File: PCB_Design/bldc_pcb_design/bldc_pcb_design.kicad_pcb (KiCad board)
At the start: 2 copper layers, 78.5 x 78.5 mm, 66 parts, among them IC1 DRV8305NPHPR, J1 Conn_01x04_Female, SW1 BOOT, SW2 RESET, U1 ESP32-WROOM-32D, U10 DS18S20Z+, U2 AS5600-ASOT, U3 LM2672M-3.3, U4 CSD18532NQ5B, U5 CSD18532NQ5B, U6 CSD18532NQ5B, U7 CSD18532NQ5B, U8 CSD18532NQ5B, U9 CSD18532NQ5B

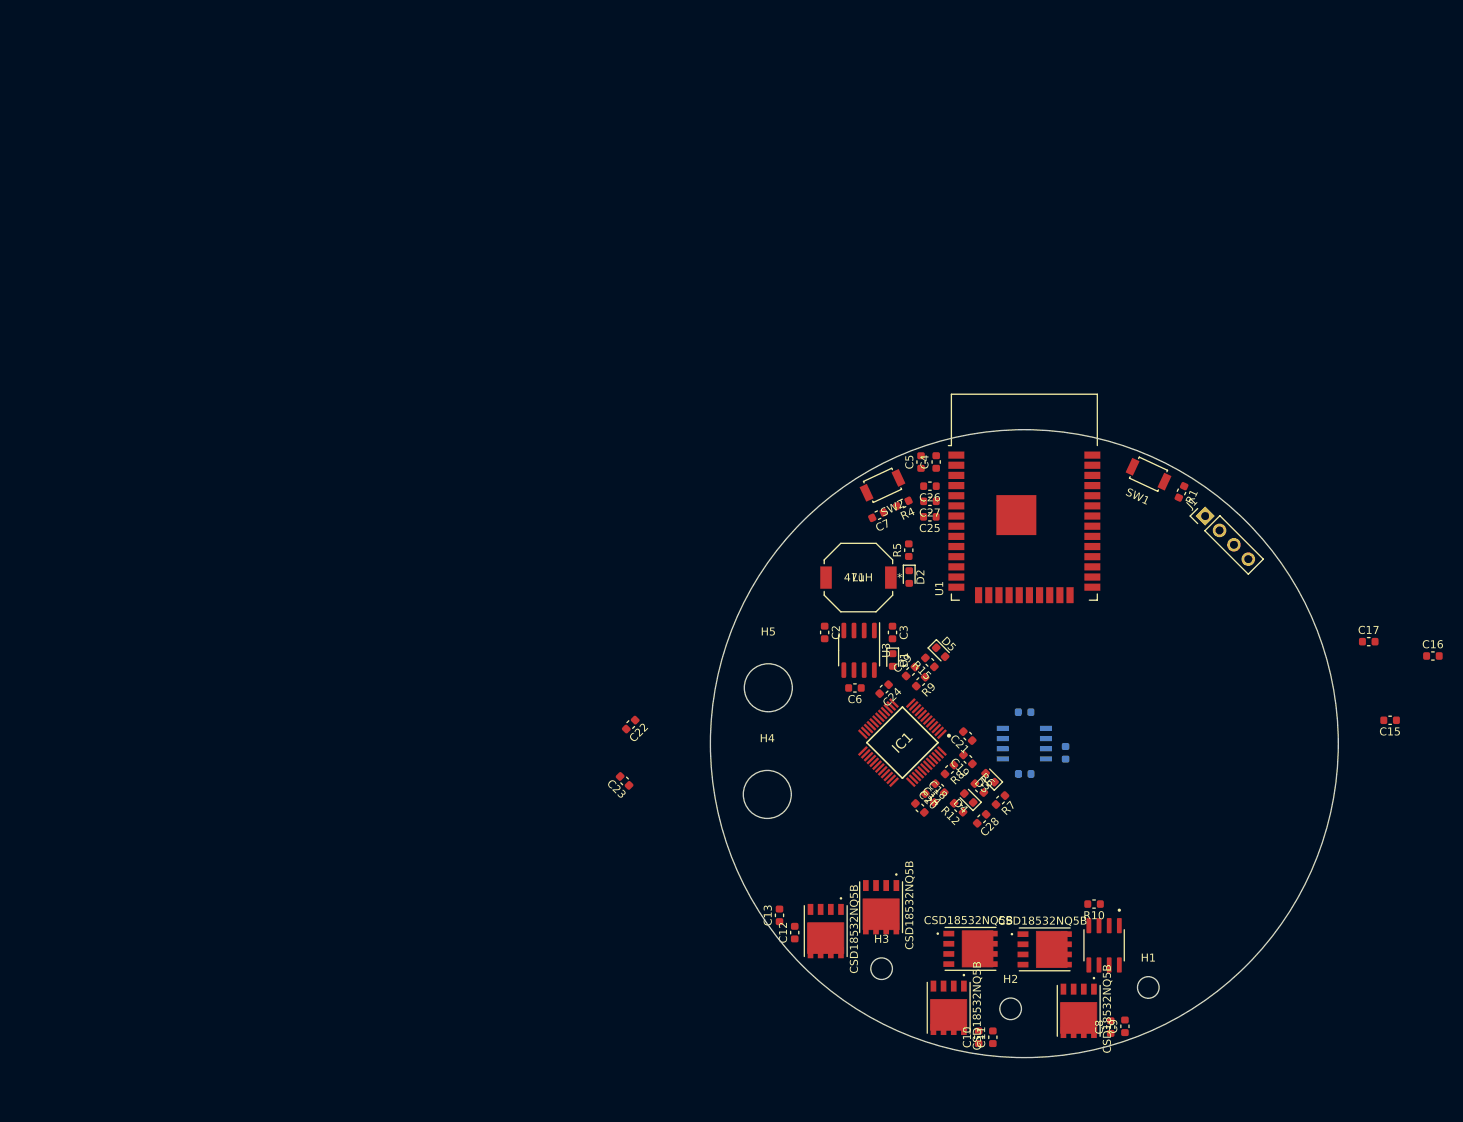
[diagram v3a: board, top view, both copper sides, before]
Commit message: Routing Iteration 1 done, Rectified schematics (SOx and shunt resistor connections)
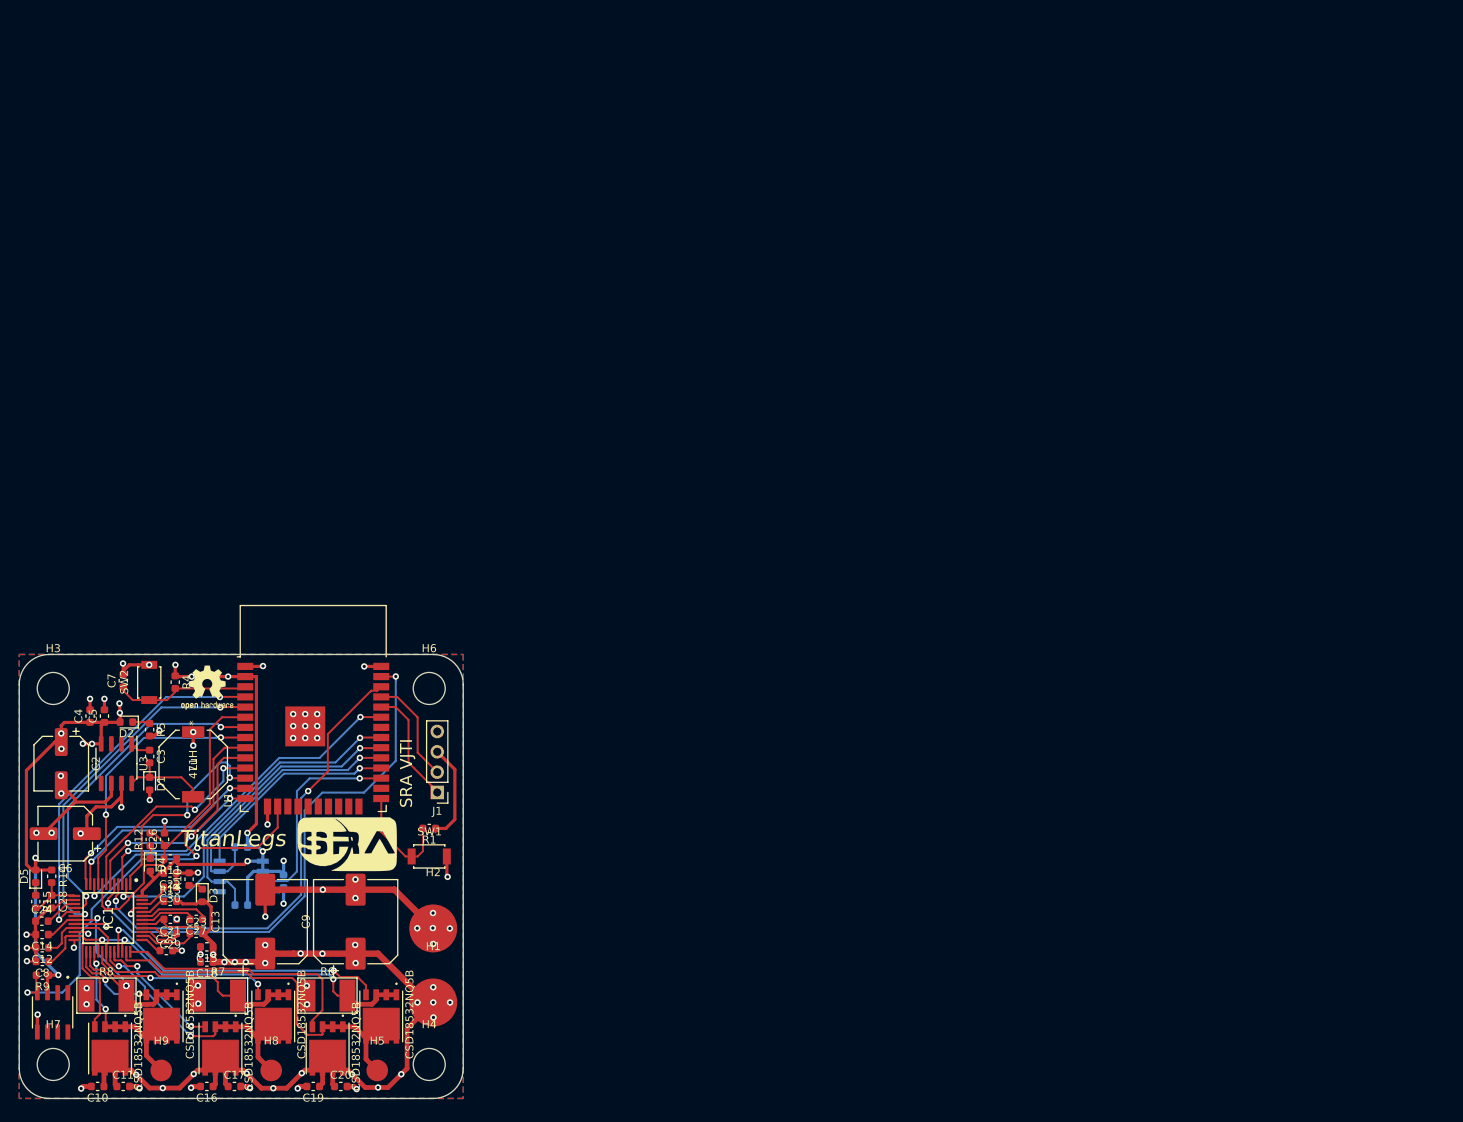
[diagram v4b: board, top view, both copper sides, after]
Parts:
- removed the C14 at (180.8, 78.5)
- removed the C19 at (184.3, 74.9)
- removed the C25 at (179.6, 44.5)
- removed the C27 at (179.6, 42.6)
- removed the C28 at (186.1, 82.3)
- removed the D3 at (187.1, 77.2)
- removed the H2 at (189.7, 106.0)
- added C11: 0.01uF, Capacitor_SMD:C_0603_1608Metric, F.Cu at (78.8, 115.8)
- added C13: 330uF 50V, Capacitor_SMD:CP_Elec_10x10, F.Cu at (96.5, 95.2)
- added C18: 10uF 50V, Capacitor_SMD:C_0603_1608Metric, F.Cu at (89.2, 100.2)
- added C21: 4.7uF, Capacitor_SMD:C_0603_1608Metric, F.Cu at (84.6, 94.9)
- added C22: 1uF 6.3V, Capacitor_SMD:C_0603_1608Metric, F.Cu at (84.6, 89.1)
- added C8: 1nF, Capacitor_SMD:C_0603_1608Metric, F.Cu at (68.6, 100.1)
- added D4: LED, Diode_SMD:D_0603_1608Metric, F.Cu at (82.1, 88.0)
- added G***: LOGO, Logos:pcb_power, B.Cu at (80.7, 102.2)
- added G***: LOGO, Logos:sralogo, B.Cu at (93.4, 72.8)
- added G***: LOGO, Logos:sralogo, F.Cu at (106.7, 85.5)
- added H3: MountingHole, MountingHole:MountingHole_4mm, F.Cu at (70.0, 66.0)
- added H4: MountingHole, MountingHole:MountingHole_4mm, F.Cu at (117.0, 113.0)
- added H6: MountingHole, MountingHole:MountingHole_4mm, F.Cu at (117.0, 66.0)
- added H7: MountingHole, MountingHole:MountingHole_4mm, F.Cu at (70.0, 113.0)
- added H8: MountingHole_Pad, MountingHole:MountingHole_2.7mm, F.Cu at (97.2, 113.8)
- added R13: 100, Resistor_SMD:R_0603_1608Metric, F.Cu at (84.6, 92.6)
- added R6: 5m, Shunt_Resistor:Shunt_Resistor_L7.0mm_B4.0mm_H1.0mm, F.Cu at (104.3, 101.9)
- added R7: 5m, Shunt_Resistor:Shunt_Resistor_L7.0mm_B4.0mm_H1.0mm, F.Cu at (90.6, 101.9)
- added REF**: KiCad-Logo2_8mm_SilkScreen, Symbol:KiCad-Logo2_8mm_SilkScreen, B.Cu at (107.7, 104.5)
- added REF**: OSHW-Logo2_7.3x6mm_SilkScreen, Symbol:OSHW-Logo2_7.3x6mm_SilkScreen, F.Cu at (89.2, 65.9)
- C15: value 1nF -> 10uF 50V
- C2: footprint Capacitor_SMD:C_0603_1608Metric -> Capacitor_SMD:CP_Elec_6.3x7.7
- C24: value 1uF 6.3V -> 1uF 6.3V
- C26: value 2.2nF -> 0.1uF
- C6: value 100uF 100V -> 100uF 50V; footprint Capacitor_SMD:C_0603_1608Metric -> Capacitor_SMD:CP_Elec_6.3x7.7
- C9: value 0.01uF -> 330uF 50V; footprint Capacitor_SMD:C_0603_1608Metric -> Capacitor_SMD:CP_Elec_10x10
- R5: value 10k -> 330
- R8: value 100 -> 5m; footprint Resistor_SMD:R_0603_1608Metric -> Shunt_Resistor:Shunt_Resistor_L7.0mm_B4.0mm_H1.0mm
- moved C12 177.6 mm to (68.6, 98.4), turned to 180 degrees
- moved C14 169.8 mm to (68.6, 96.8), turned to 180 degrees
- moved C15 150.6 mm to (89.2, 98.3)
- moved R9 131.7 mm to (68.7, 101.8)
- moved U10 131.7 mm to (69.9, 106.5)
- moved C10 126.9 mm to (75.5, 115.8), turned to 180 degrees
- moved D5 116.5 mm to (67.8, 89.5), turned to 90 degrees
- moved R15 115.7 mm to (67.8, 92.6), turned to 270 degrees
- moved R14 111.3 mm to (69.8, 89.5), turned to 270 degrees
- moved C28 111.1 mm to (69.8, 92.6), turned to 270 degrees
- moved C4 110.4 mm to (74.6, 69.5)
- moved C24 109.2 mm to (68.6, 95.1), turned to 0 degrees
- moved R8 108.5 mm to (76.7, 101.9), turned to 180 degrees
- moved C5 106.9 mm to (76.4, 69.5)
- moved R12 106.4 mm to (82.1, 84.9), turned to 90 degrees
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- renumbered C8 to C10, C16 to C12, C17 to C14, C10 to C16, C11 to C17, C12 to C19, C13 to C20, C18 to C23, C20 to C25, C22 to C27, C29 to C28, C23 to C29, C21 to C30, D4 to D3, H4 to H1, H5 to H2, H1 to H5, H3 to H9, R12 to R10, R6 to R11, R7 to R12, R9 to R14, R10 to R9
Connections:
- C15 pad 1: SLA -> POWER_IN
- C26 pad 1: ISENB -> DRV_nFAULT
- IC1 pad 16: SO1 -> ISENA
- IC1 pad 17: SO2 -> ISENB
- IC1 pad 18: SO3 -> ISENC
- R8 pad 1: VDRAIN -> SLC
- R8 pad 2: POWER_IN -> GND
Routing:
- net 3V3_IN: track 0.00 -> 140.9 mm, vias 0 -> 17
- net POWER_IN: track 0.00 -> 130.7 mm, vias 0 -> 26
- net GND: track 0.00 -> 108.5 mm, vias 0 -> 58
- net DRV_LB: track 0.00 -> 68.0 mm, vias 0 -> 2
- net DRV_HB: track 0.00 -> 59.6 mm, vias 0 -> 2
- net TEMP_DQ: track 0.00 -> 54.3 mm, vias 0 -> 2
- net SLA: track 0.00 -> 53.3 mm, vias 0 -> 3
- net MOT_A: track 0.00 -> 47.9 mm
- net ISENB: track 0.00 -> 45.6 mm, vias 0 -> 2
- net DRV_HA: track 0.00 -> 45.0 mm, vias 0 -> 2
- net ISENC: track 0.00 -> 44.7 mm, vias 0 -> 2
- net DRV_LA: track 0.00 -> 43.0 mm, vias 0 -> 2
- net ISENA: track 0.00 -> 41.4 mm, vias 0 -> 2
- net DRV_nFAULT: track 0.00 -> 41.2 mm
- net SLB: track 0.00 -> 40.0 mm
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- added copper zone on B.Cu, net (none)
- added copper zone on F.Cu, net (none)
- added copper zone on In2.Cu, net 3V3_IN
- added copper zone on In1.Cu, net GND
- added copper zone on In2.Cu, net POWER_IN
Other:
- board size 78.5 x 78.5 mm -> 55.5 x 55.5 mm
- copper layers 2 -> 4
- board text added: "SRA VJTI"
- board text added: "SRA-VJTI"
- board text added: "Society of Robotics & Automation"
- board text added: "TitanLegs"

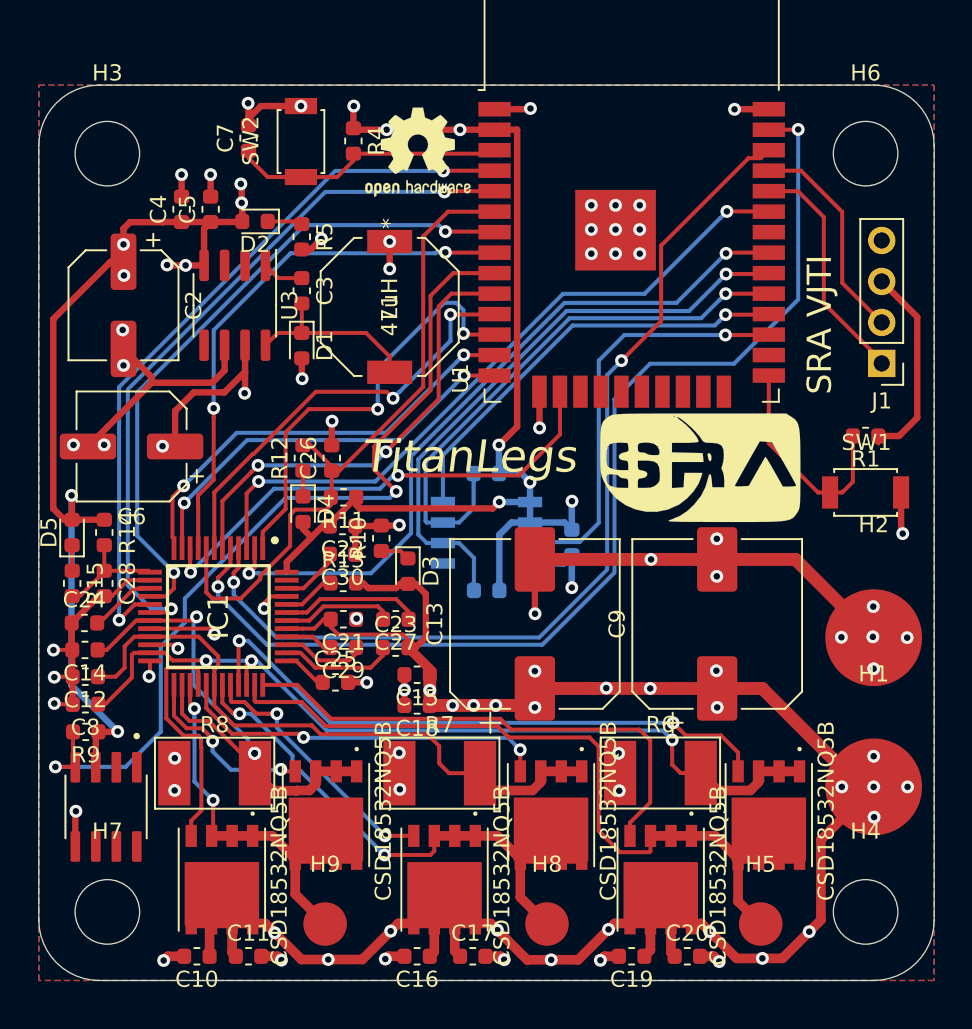
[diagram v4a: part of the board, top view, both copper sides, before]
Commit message: Made routing changes and optimized schematics, pcbnew
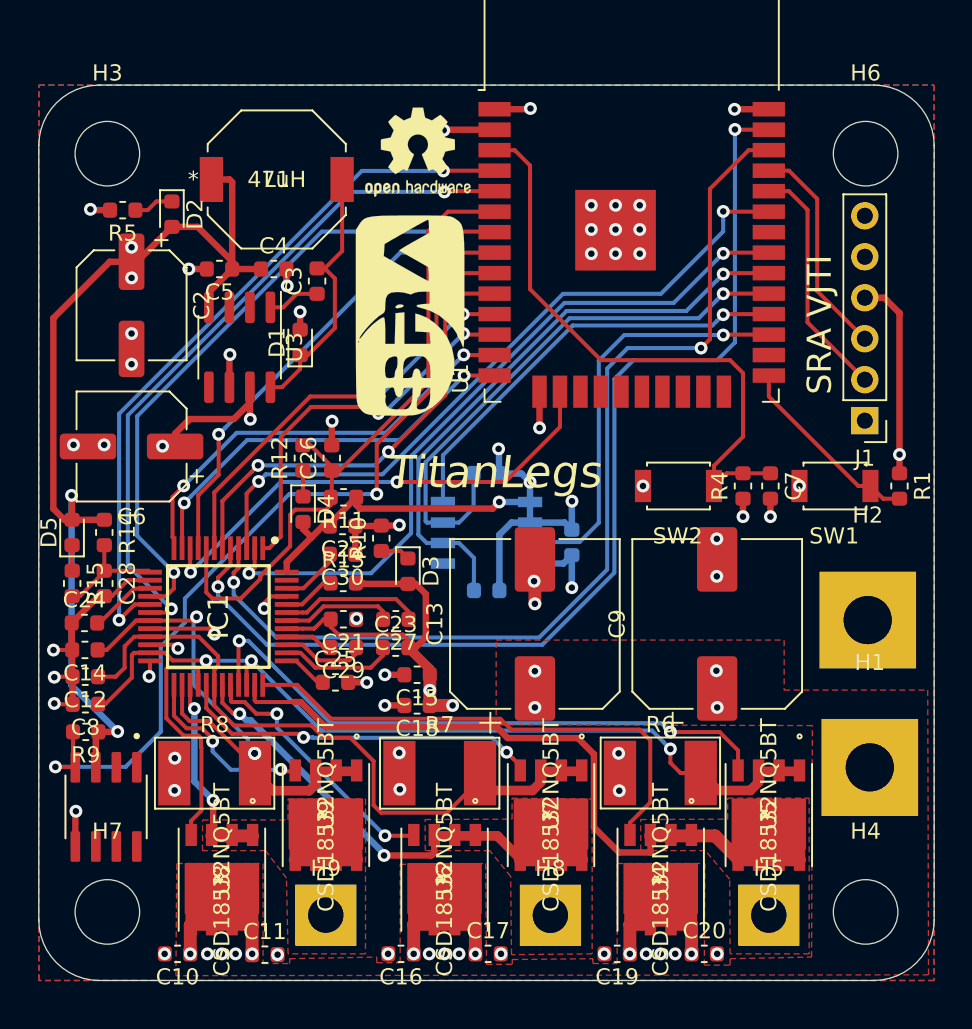
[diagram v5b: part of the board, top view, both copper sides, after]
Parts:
- H1, H2: footprint MountingHole:MountingHole_6mm -> MountingHole:MountingHole_6.4mm_M6_DIN965_Pad
- H5, H8, H9: footprint MountingHole:MountingHole_2.7mm -> MountingHole:MountingHole_2.2mm_M2_DIN965_Pad
- J1: value Conn_01x04_Female -> Conn_01x06_Female; footprint Connector_PinHeader_2.54mm:PinHeader_1x04_P2.54mm_Vertical -> Connector_PinHeader_2.54mm:PinHeader_1x06_P2.54mm_Vertical
- U4, U5, U6, U7, U8, U9: value CSD18532NQ5B -> CSD18532NQ5BT
- moved C7 38.9 mm to (111.1, 86.6), turned to 270 degrees
- moved R4 32.3 mm to (109.4, 86.6), turned to 90 degrees
- moved SW2 31.7 mm to (105.4, 86.6), turned to 0 degrees
- moved G*** 20.2 mm to (88.8, 76.1), turned to 90 degrees
- moved R5 11.2 mm to (71.0, 69.5), turned to 180 degrees
- moved L1 10.6 mm to (80.5, 67.6), turned to 0 degrees
- moved C4 6.81 mm to (80.3, 73.2), turned to 0 degrees
- moved D2 5.17 mm to (74.0, 69.8), turned to 270 degrees
- moved R1 3.74 mm to (119.1, 86.6), turned to 270 degrees
- moved C5 3.74 mm to (77.0, 73.2), turned to 180 degrees
- moved J1 3.70 mm to (117.0, 82.5)
- moved U3 2.62 mm to (78.2, 78.0)
- moved SW1 1.94 mm to (115.1, 86.6), turned to 0 degrees
- moved H1 1.23 mm to (117.3, 104.0)
- moved C10 1.21 mm to (74.3, 115.6)
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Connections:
- J1 pad 1: RX -> DTR
- J1 pad 2: TX -> RX
- J1 pad 3: 3V3_IN -> TX
- J1 pad 4: GND -> 3V3_IN
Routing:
- net POWER_IN: track 130.7 -> 54.2 mm, vias 26 -> 23
- net GND: track 108.5 -> 57.0 mm, vias 58 -> 55
- net 3V3_IN: track 140.9 -> 114.9 mm, vias 17 -> 11
- net RESET: track 17.1 -> 37.5 mm
- net MOT_C: track 24.4 -> 16.4 mm
- net Net-(C3-Pad2): track 11.4 -> 16.4 mm
- net MOT_A: track 47.9 -> 43.1 mm
- net MOT_B: track 33.9 -> 29.1 mm
- net DRV_SPI_nSCS: track 33.3 -> 29.4 mm
- net DRV_EN_GATE: track 27.2 -> 23.8 mm
- net SLB: track 40.0 -> 43.2 mm
- net DRV_HB: track 59.6 -> 62.6 mm
- net BOOT: track 13.8 -> 12.0 mm
- net TEMP_DQ: track 54.3 -> 52.6 mm
- net ISENC: track 44.7 -> 43.0 mm
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- added copper zone on F.Cu, net MOT_A
- added copper zone on F.Cu, net MOT_B
- added copper zone on F.Cu, net MOT_C
- added copper zone on F.Cu, net POWER_IN

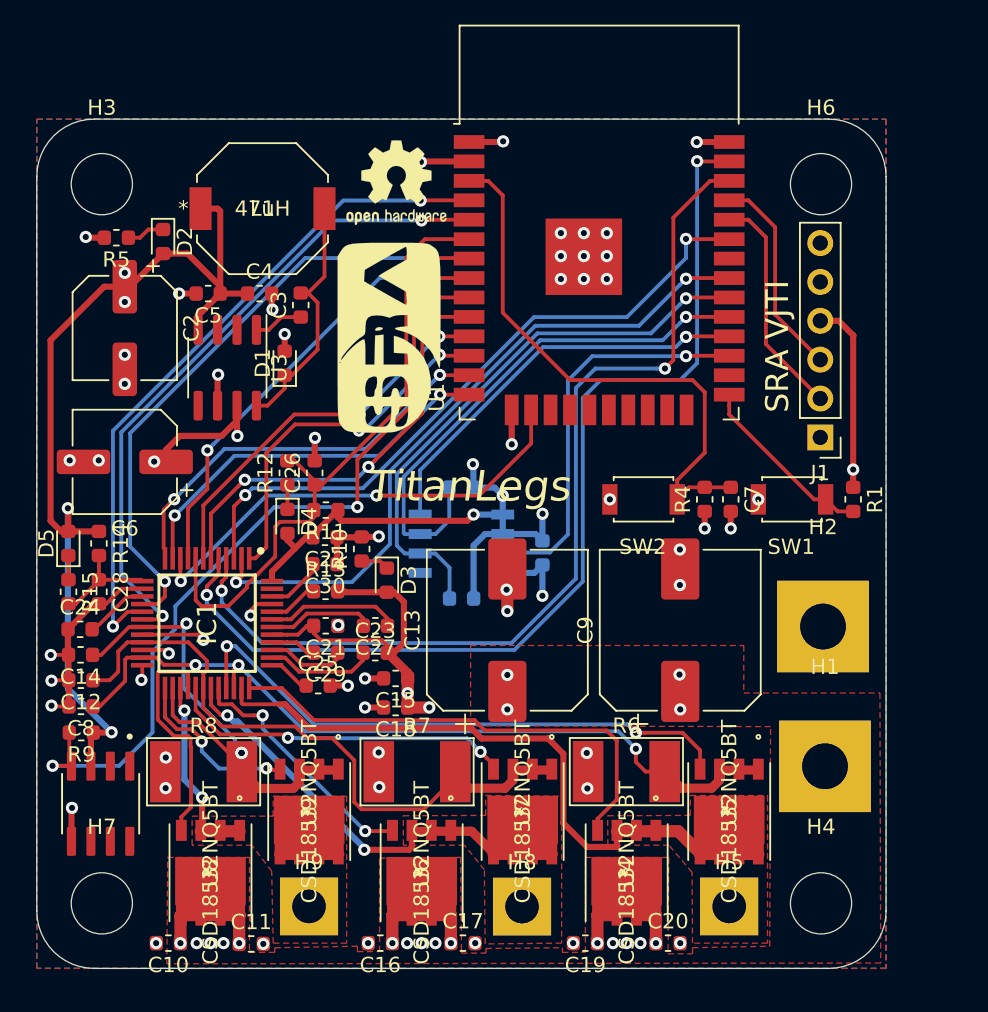
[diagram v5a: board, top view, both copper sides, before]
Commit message: Minor Silkscreen changes
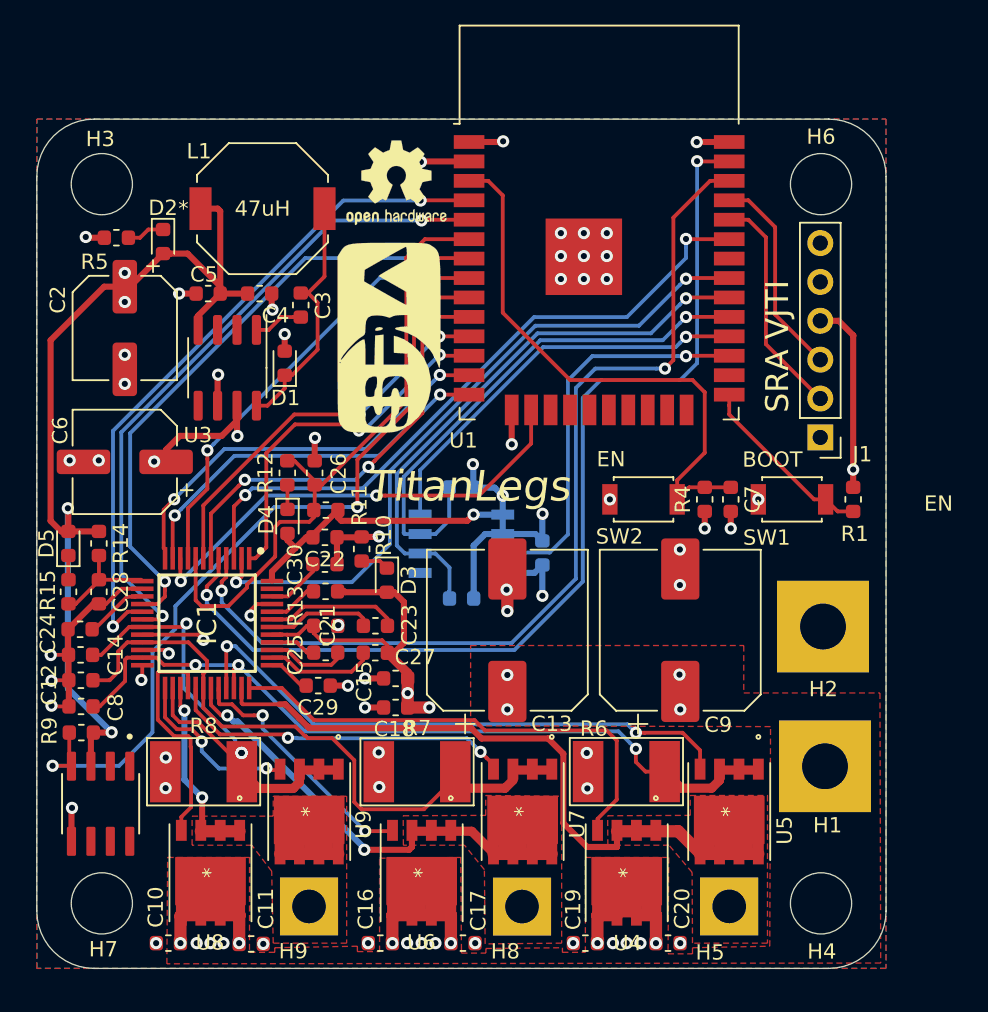
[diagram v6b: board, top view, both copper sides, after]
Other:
- board text added: "BOOT"
- board text added: "EN"
